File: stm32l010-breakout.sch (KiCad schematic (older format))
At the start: 27 parts, among them J1 SWD, J2 Left, J3 Right, Q1 BC847BS, SW1 Reset, U1 STM32L010K8Tx, Y1 32.768kHz

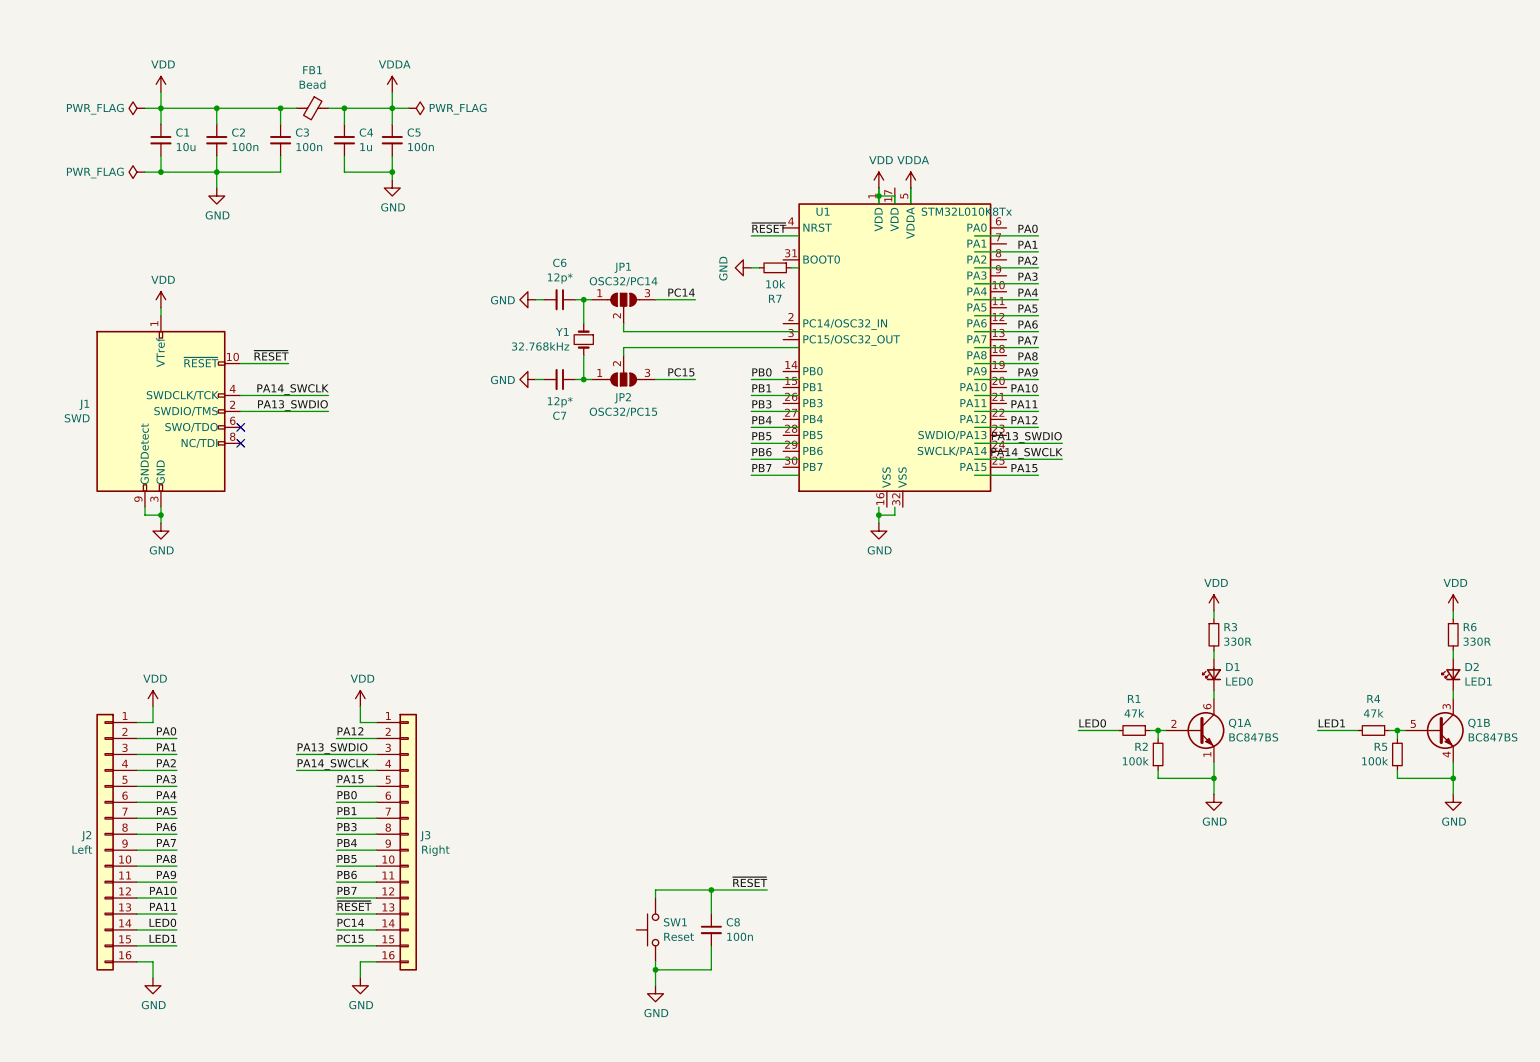
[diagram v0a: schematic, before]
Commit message: Schematic cleanup, partial re-layout
- Changed the PCB size to 25x50mm
- Use 0R resistors for LSE oscillator/GPIO selection
- Schematic cleanup
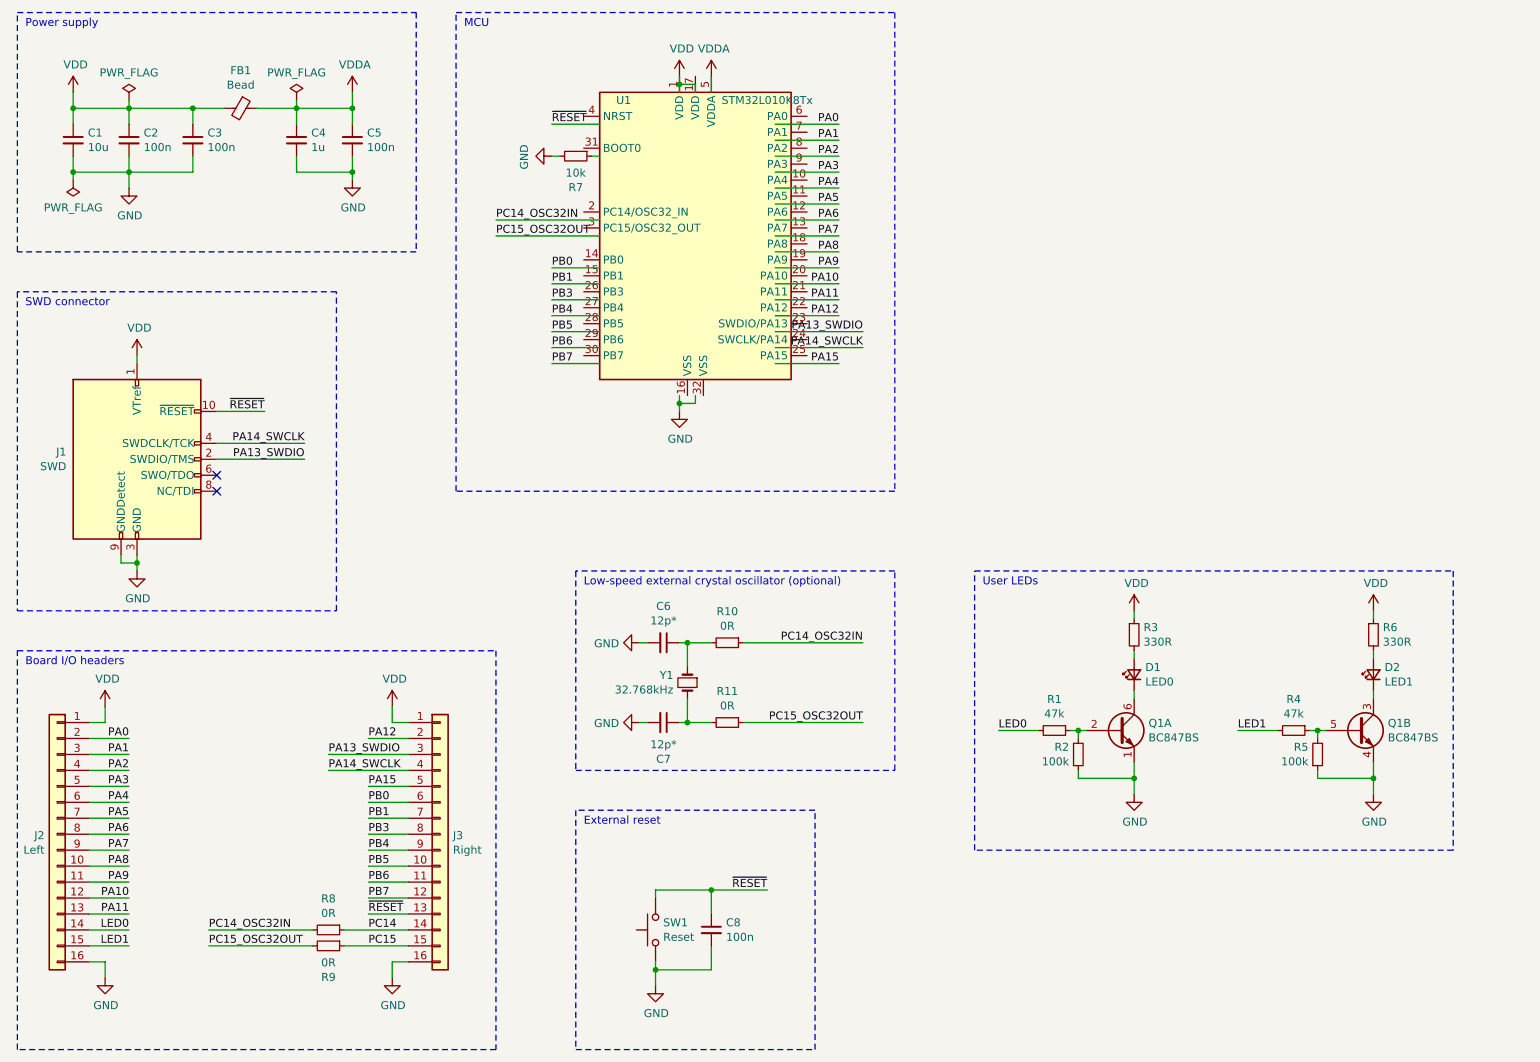
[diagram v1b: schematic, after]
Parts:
- removed JP1: OSC32/PC14, Jumper:SolderJumper-3_P1.3mm_Open_RoundedPad1.0x1.5mm_NumberLabels, symbol Jumper:SolderJumper_3_Open
- removed JP2: OSC32/PC15, Jumper:SolderJumper-3_P1.3mm_Open_RoundedPad1.0x1.5mm_NumberLabels, symbol Jumper:SolderJumper_3_Open
- added R10, R11, R8, R9: 0R, Resistor_SMD:R_0603_1608Metric, symbol Device:R_Small
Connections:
- net labels added: PC14_OSC32IN, PC15_OSC32OUT
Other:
- note added: "Board I/O headers"
- note added: "External reset"
- note added: "Low-speed external crystal oscillator (optional)"
- note added: "MCU"
- note added: "Power supply"
- note added: "SWD connector"
- note added: "User LEDs"
- moved on the sheet: C1, C2, C3, C4, C5, C6, C7, D1, D2, FB1, J1, J2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

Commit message: Finished laying out Revision B
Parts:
- Q1: value BC847BS -> BC847CDW1
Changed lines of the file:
@@
 Sheet 1 1
 Title "STM32L010 Breakout Board"
-Date "2020-07-30"
+Date "2020-08-14"
 Rev "B"
 Comp "Michal Potrzebicz"
-Comment1 "https://creativecommons.org/licenses/by-sa/4.0/"
-Comment2 "Released under the CC BY-SA 4.0 License"
-Comment3 "most of the STM32L0 and STM32L4 chips in LQFP-32 packages"
-Comment4 "Universal STM32L010 breakout board compatible also with"
+Comment1 "other STM32L0 and STM32L4 chips in LQFP-32 packages"
+Comment2 "Universal STM32L010 breakout board compatible also with"
+Comment3 ""
+Comment4 "License: CC BY-SA 4.0"
 $EndDescr
 $Comp
@@
 P 9400 5500
 F 0 "Q1" H 9590 5546 50  0000 L CNN
-F 1 "BC847BS" H 9590 5455 50  0000 L CNN
+F 1 "BC847CDW1" H 9590 5455 50  0000 L CNN
 F 2 "Package_TO_SOT_SMD:SOT-363_SC-70-6" H 9600 5600 50  0001 C CNN
 F 3 "https://assets.nexperia.com/documents/data-sheet/BC847BS.pdf" H 9400 5500 50  0001 C CNN
@@
 P 7900 5500
 F 0 "Q1" H 8090 5546 50  0000 L CNN
-F 1 "BC847BS" H 8090 5455 50  0000 L CNN
+F 1 "BC847CDW1" H 8090 5455 50  0000 L CNN
 F 2 "Package_TO_SOT_SMD:SOT-363_SC-70-6" H 8100 5600 50  0001 C CNN
 F 3 "https://assets.nexperia.com/documents/data-sheet/BC847BS.pdf" H 7900 5500 50  0001 C CNN
@@
 External reset
 Wire Notes Line
-	10000 6250 7000 6250
+	10100 6250 7000 6250
 Wire Notes Line
 	7000 6250 7000 4500
 Wire Notes Line
-	7000 4500 10000 4500
-Wire Notes Line
-	10000 4500 10000 6250
+	7000 4500 10100 4500
+Wire Notes Line
+	10100 4500 10100 6250
 Text Notes 7050 4600 0    50   ~ 0
 User LEDs

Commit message: Schematic cleanup
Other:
- note added: "C6 and C7 must match the Y1 specs\n\nR10 and R11 placed only if the LSE crystal is in use"
- note added: "R8 and R9 placed only when the LSE crystal is not populated"
- moved on the sheet: C6, C7, C8, J2, J3, R10, R11, R7, R8, R9, SW1, U1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

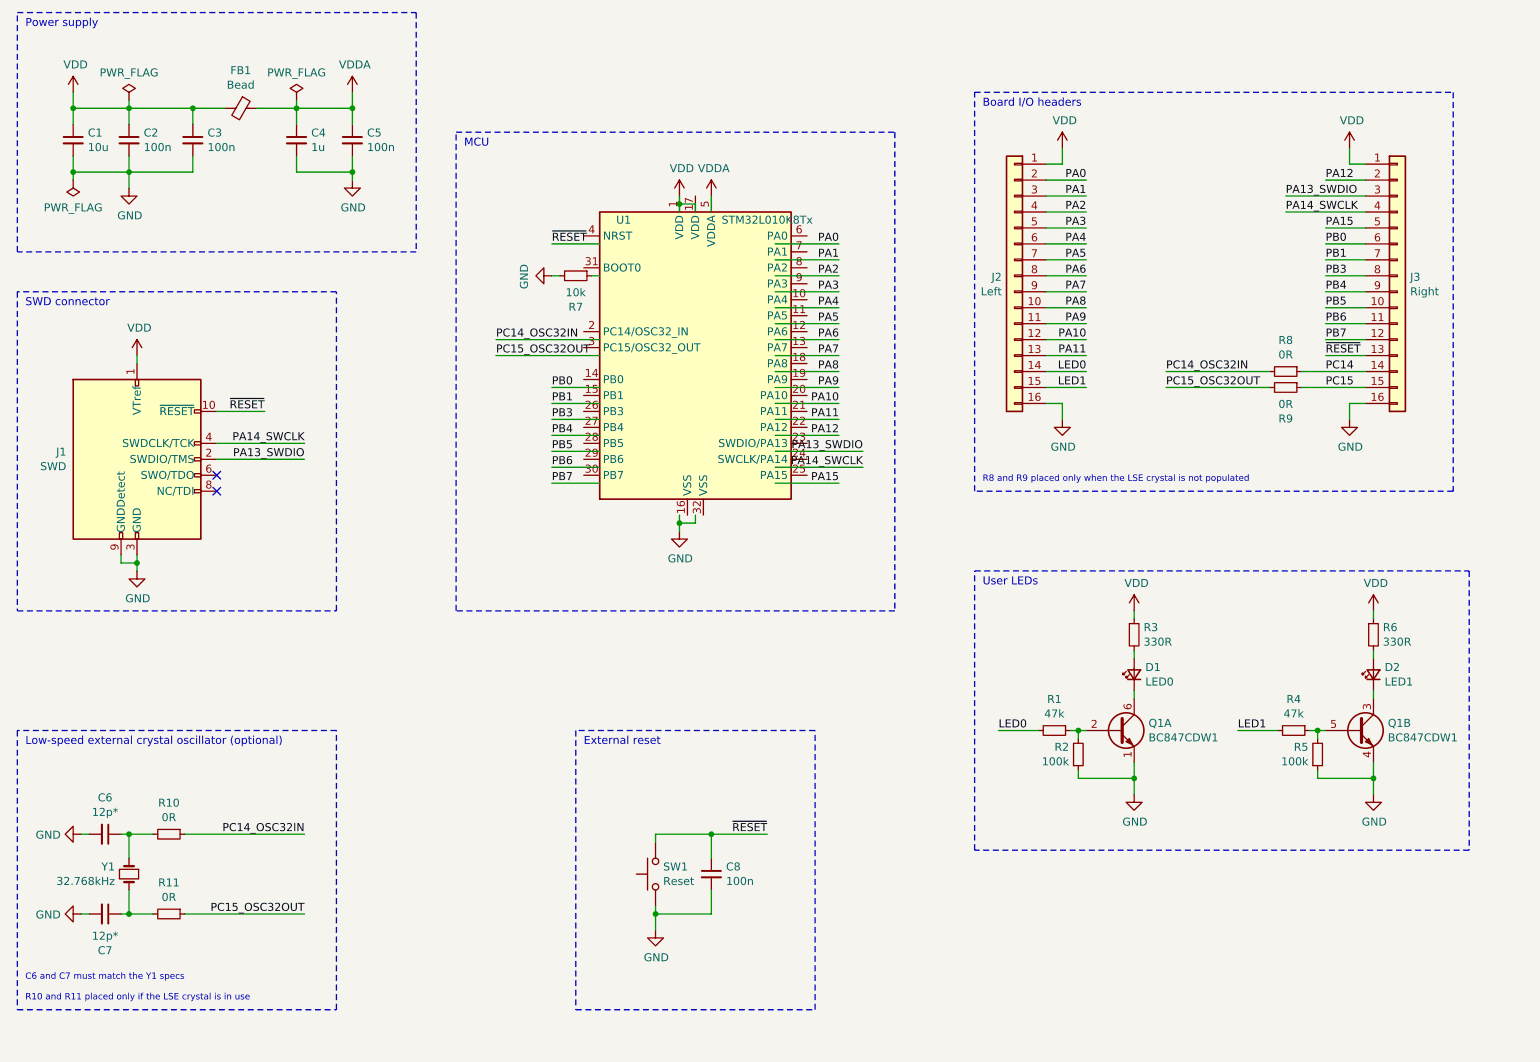
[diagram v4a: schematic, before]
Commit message: Updated STM32L010 symbol
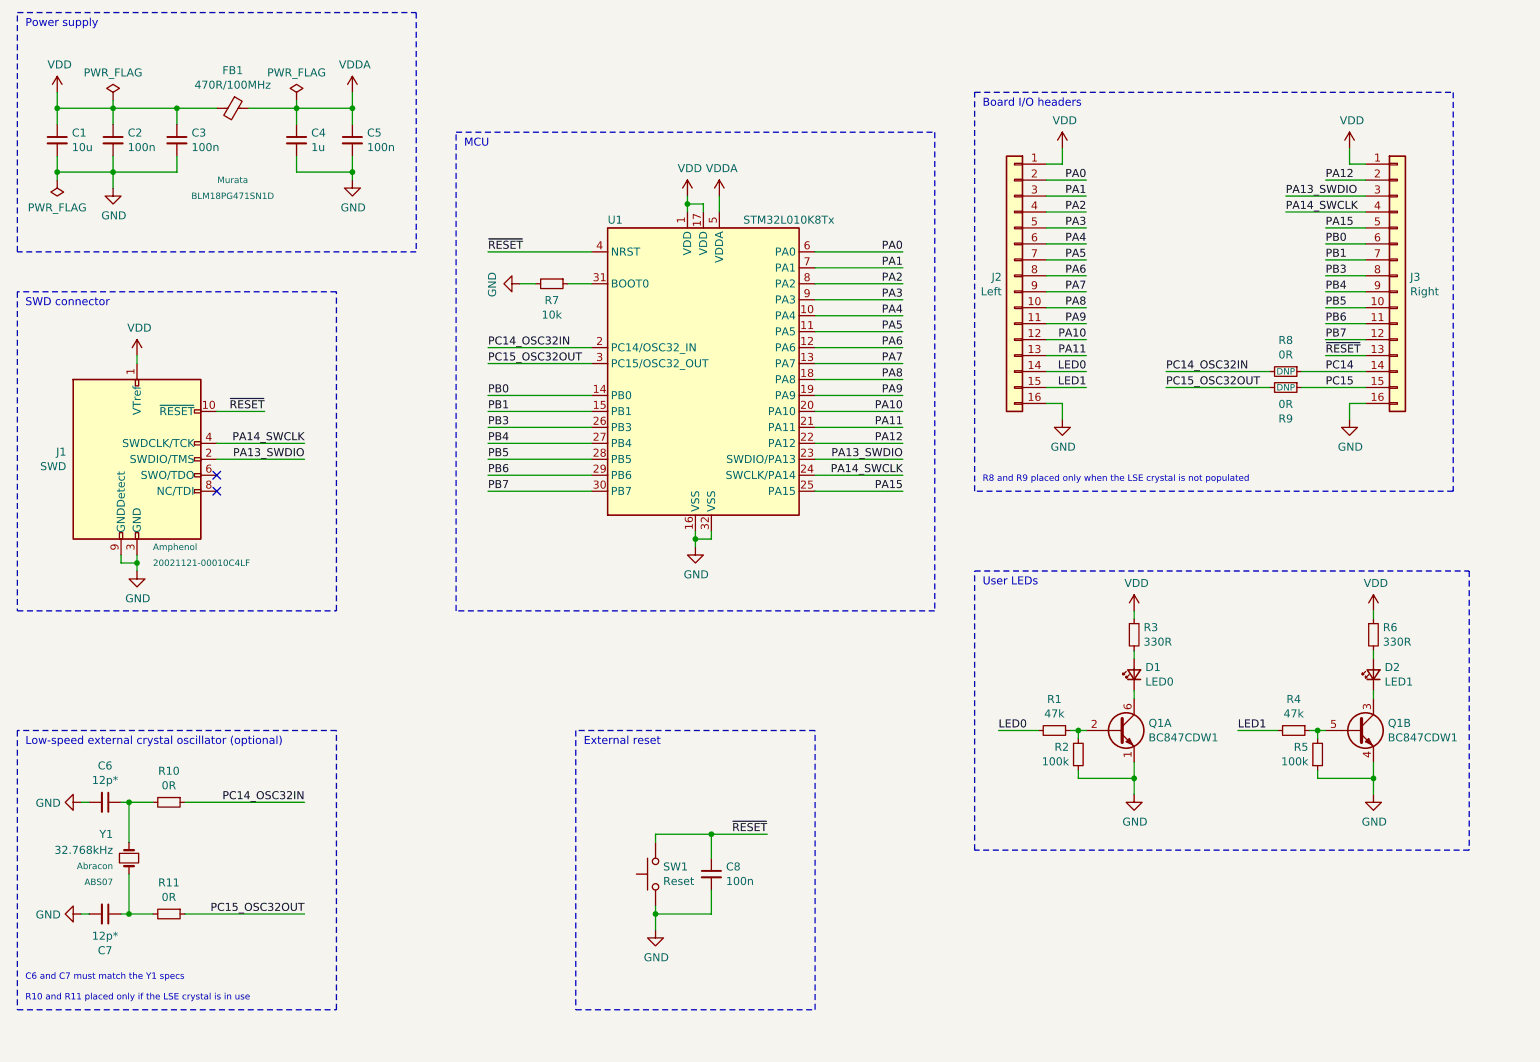
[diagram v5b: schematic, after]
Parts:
- FB1: value Bead -> 470R/100MHz; MFR (none) -> Murata; MPN (none) -> BLM18PG471SN1D
- J1: MFR (none) -> Amphenol; MPN (none) -> 20021121-00010C4LF
- R8, R9: DNP (none) -> DNP
- U1: MFR (none) -> ST; MPN (none) -> STM32L010K8T6
- Y1: MFR (none) -> Abracon; MPN (none) -> ABS07
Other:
- moved on the sheet: C1, C2, C3, C6, FB1, R10, R7, U1, Y1

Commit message: Synced with library changes
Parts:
- U1: symbol Elevendroids_MCU_ST:STM32L010K8Tx -> Elevendroids_MCU_ST_STM32L0:STM32L010K8Tx
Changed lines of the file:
@@
 	4600 2700 4450 2700
 $Comp
-L Elevendroids_MCU_ST:STM32L010K8Tx U1
+L Elevendroids_MCU_ST_STM32L0:STM32L010K8Tx U1
 U 1 1 5F20ADE9
 P 5300 3250
